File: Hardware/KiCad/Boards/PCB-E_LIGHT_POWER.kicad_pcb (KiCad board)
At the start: 2 copper layers, 110 x 94 mm, 0 parts

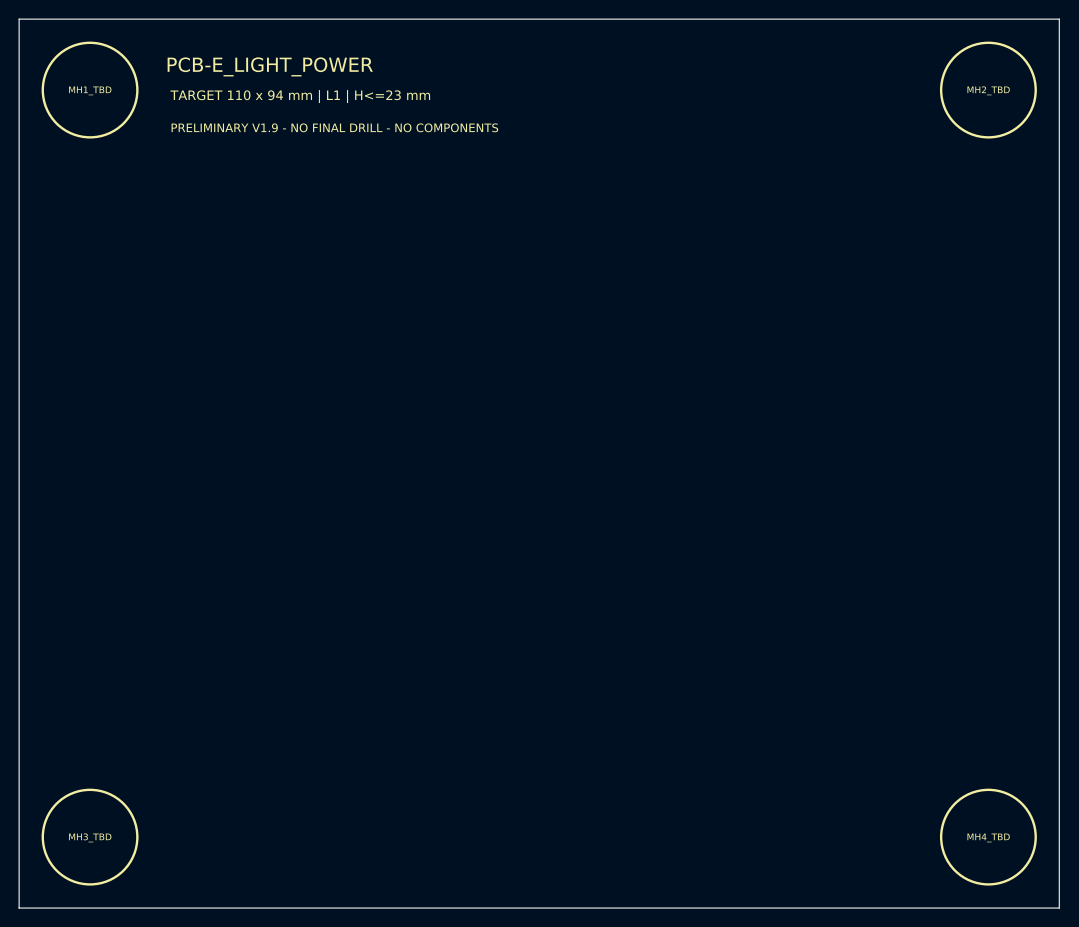
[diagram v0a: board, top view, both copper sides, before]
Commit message: hardware: add PCB-E functional, height and thermal placeholders
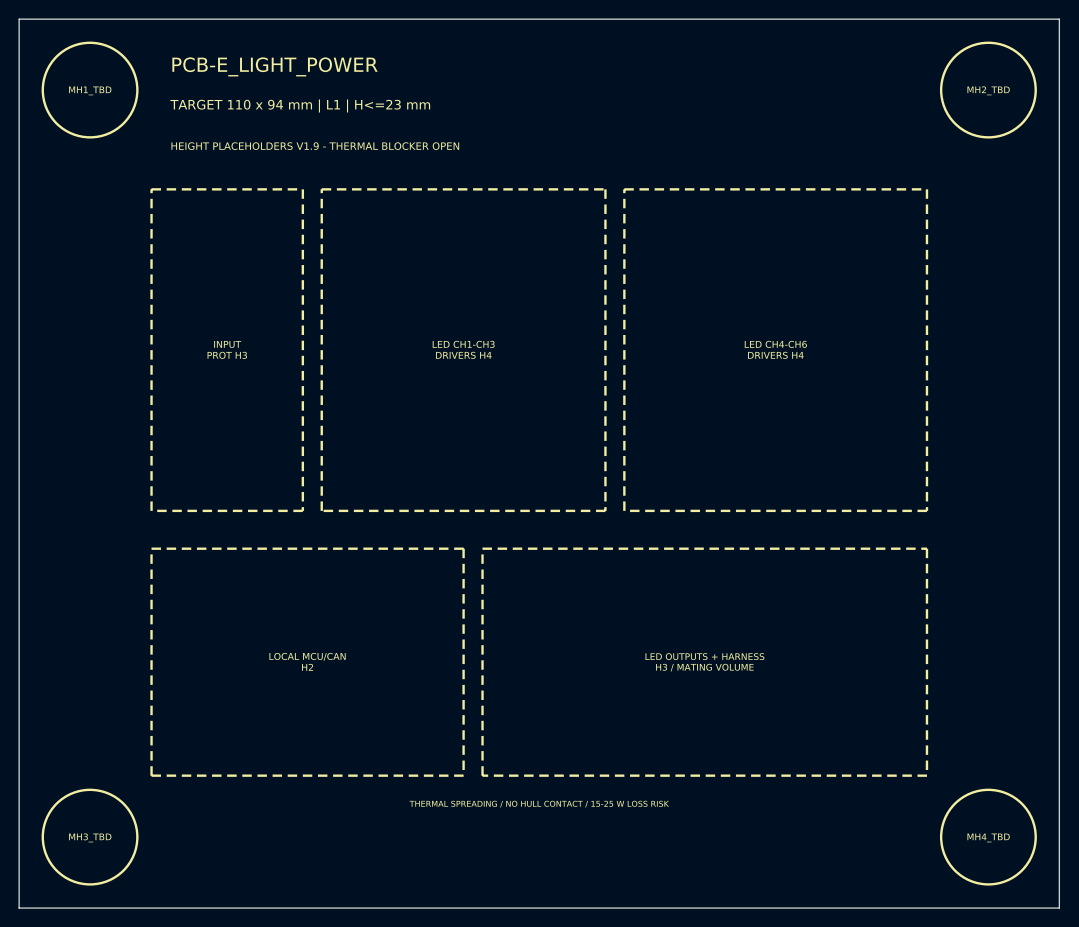
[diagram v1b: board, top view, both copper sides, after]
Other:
- board text added: "HEIGHT PLACEHOLDERS V1.9 - THERMAL BLOCKER OPEN"
- board text added: "INPUT PROT H3"
- board text added: "LED CH1-CH3 DRIVERS H4"
- board text added: "LED CH4-CH6 DRIVERS H4"
- board text added: "LED OUTPUTS + HARNESS H3 / MATING VOLUME"
- board text added: "LOCAL MCU/CAN H2"
- board text added: "THERMAL SPREADING / NO HULL CONTACT / 15-25 W LOSS RISK"
- board text removed: "PRELIMINARY V1.9 - NO FINAL DRILL - NO COMPONENTS"
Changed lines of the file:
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@@
 		(pad_to_mask_clearance 0)
 		(allow_soldermask_bridges_in_footprints no)
-		(tenting
-			(front yes)
-			(back yes)
-		)
-		(covering
-			(front no)
-			(back no)
-		)
-		(plugging
-			(front no)
-			(back no)
-		)
-		(capping no)
-		(filling no)
-		(pcbplotparams
-			(layerselection 0x00000000_00000000_55555555_5755f5ff)
-			(plot_on_all_layers_selection 0x00000000_00000000_00000000_00000000)
-			(disableapertmacros no)
-			(usegerberextensions no)
-			(usegerberattributes yes)
-			(usegerberadvancedattributes yes)
-			(creategerberjobfile yes)
-			(dashed_line_dash_ratio 12)
-			(dashed_line_gap_ratio 3)
-			(svgprecision 4)
-			(plotframeref no)
-			(mode 1)
-			(useauxorigin no)
-			(pdf_front_fp_property_popups yes)
-			(pdf_back_fp_property_popups yes)
-			(pdf_metadata yes)
-			(pdf_single_document no)
-			(dxfpolygonmode yes)
-			(dxfimperialunits yes)
-			(dxfusepcbnewfont yes)
-			(psnegative no)
-			(psa4output no)
-			(plot_black_and_white yes)
-			(sketchpadsonfab no)
-			(plotpadnumbers no)
-			(hidednponfab no)
-			(sketchdnponfab yes)
-			(crossoutdnponfab yes)
-			(subtractmaskfromsilk no)
-			(outputformat 1)
-			(mirror no)
-			(drillshape 1)
-			(scaleselection 1)
-			(outputdirectory "")
-		)
 	)
-	(gr_circle
-		(center 27.5 27.5)
-		(end 32.5 27.5)
-		(stroke
-			(width 0.25)
-			(type dash)
-		)
-		(fill no)
-		(layer "F.SilkS")
-	)
-	(gr_circle
-		(center 27.5 106.5)
-		(end 32.5 106.5)
-		(stroke
-			(width 0.25)
-			(type dash)
-		)
-		(fill no)
-		(layer "F.SilkS")
-	)
-	(gr_circle
-		(center 122.5 27.5)
-		(end 127.5 27.5)
-		(stroke
-			(width 0.25)
-			(type dash)
-		)
-		(fill no)
-		(layer "F.SilkS")
-	)
-	(gr_circle
-		(center 122.5 106.5)
-		(end 127.5 106.5)
-		(stroke
-			(width 0.25)
-			(type dash)
-		)
-		(fill no)
-		(layer "F.SilkS")
-	)
-	(gr_rect
-		(start 20 20)
-		(end 130 114)
-		(stroke
-			(width 0.05)
-			(type default)
-		)
-		(fill no)
-		(layer "Edge.Cuts")
-	)
-	(gr_text "MH1_TBD"
-		(at 27.5 27.5 0)
-		(layer "F.SilkS")
-		(effects
-			(font
-				(size 0.7 0.7)
-				(thickness 0.14)
-			)
-		)
-	)
-	(gr_text "MH3_TBD"
-		(at 27.5 106.5 0)
-		(layer "F.SilkS")
-		(effects
-			(font
-				(size 0.7 0.7)
-				(thickness 0.14)
-			)
-		)
-	)
-	(gr_text "MH2_TBD"
-		(at 122.5 27.5 0)
-		(layer "F.SilkS")
-		(effects
-			(font
-				(size 0.7 0.7)
-				(thickness 0.14)
-			)
-		)
-	)
-	(gr_text "MH4_TBD"
-		(at 122.5 106.5 0)
-		(layer "F.SilkS")
-		(effects
-			(font
-				(size 0.7 0.7)
-				(thickness 0.14)
-			)
-		)
-	)
-	(gr_text "PRELIMINARY V1.9 - NO FINAL DRILL - NO COMPONENTS"
-		(at 36 31 0)
-		(layer "F.SilkS")
-		(effects
-			(font
-				(size 0.9 0.9)
-				(thickness 0.18)
-			)
-			(justify left top)
-		)
-	)
-	(gr_text "TARGET 110 x 94 mm | L1 | H<=23 mm"
-		(at 36 27.5 0)
-		(layer "F.SilkS")
-		(effects
-			(font
-				(size 1 1)
-				(thickness 0.2)
-			)
-			(justify left top)
-		)
-	)
-	(gr_text "PCB-E_LIGHT_POWER"
-		(at 35.5 24 0)
-		(layer "F.SilkS")
-		(effects
-			(font
-				(size 1.5 1.5)
-				(thickness 0.3)
-			)
-			(justify left top)
-		)
-	)
+	(gr_rect (start 20 20) (end 130 114) (stroke (width 0.05) (type default)) (fill no) (layer "Edge.Cuts"))
+	(gr_text "PCB-E_LIGHT_POWER" (at 36 24 0) (layer "F.SilkS") (effects (font (size 1.5 1.5) (thickness 0.3)) (justify left top)))
+	(gr_text "TARGET 110 x 94 mm | L1 | H<=23 mm" (at 36 28.5 0) (layer "F.SilkS") (effects (font (size 1 1) (thickness 0.2)) (justify left top)))
+	(gr_text "HEIGHT PLACEHOLDERS V1.9 - THERMAL BLOCKER OPEN" (at 36 33 0) (layer "F.SilkS") (effects (font (size 0.78 0.78) (thickness 0.15)) (justify left top)))
+	(gr_circle (center 27.5 27.5) (end 32.5 27.5) (stroke (width 0.25) (type dash)) (fill no) (layer "F.SilkS"))
+	(gr_circle (center 27.5 106.5) (end 32.5 106.5) (stroke (width 0.25) (type dash)) (fill no) (layer "F.SilkS"))
+	(gr_circle (center 122.5 27.5) (end 127.5 27.5) (stroke (width 0.25) (type dash)) (fill no) (layer "F.SilkS"))
+	(gr_circle (center 122.5 106.5) (end 127.5 106.5) (stroke (width 0.25) (type dash)) (fill no) (layer "F.SilkS"))
+	(gr_text "MH1_TBD" (at 27.5 27.5 0) (layer "F.SilkS") (effects (font (size 0.7 0.7) (thickness 0.14))))
+	(gr_text "MH2_TBD" (at 122.5 27.5 0) (layer "F.SilkS") (effects (font (size 0.7 0.7) (thickness 0.14))))
+	(gr_text "MH3_TBD" (at 27.5 106.5 0) (layer "F.SilkS") (effects (font (size 0.7 0.7) (thickness 0.14))))
+	(gr_text "MH4_TBD" (at 122.5 106.5 0) (layer "F.SilkS") (effects (font (size 0.7 0.7) (thickness 0.14))))
+	(gr_rect (start 34 38) (end 50 72) (stroke (width 0.25) (type dash)) (fill no) (layer "F.SilkS"))
+	(gr_text "INPUT\nPROT H3" (at 42 55 0) (layer "F.SilkS") (effects (font (size 0.72 0.72) (thickness 0.13))))
+	(gr_rect (start 52 38) (end 82 72) (stroke (width 0.25) (type dash)) (fill no) (layer "F.SilkS"))
+	(gr_text "LED CH1-CH3\nDRIVERS H4" (at 67 55 0) (layer "F.SilkS") (effects (font (size 0.72 0.72) (thickness 0.13))))
+	(gr_rect (start 84 38) (end 116 72) (stroke (width 0.25) (type dash)) (fill no) (layer "F.SilkS"))
+	(gr_text "LED CH4-CH6\nDRIVERS H4" (at 100 55 0) (layer "F.SilkS") (effects (font (size 0.72 0.72) (thickness 0.13))))
+	(gr_rect (start 34 76) (end 67 100) (stroke (width 0.25) (type dash)) (fill no) (layer "F.SilkS"))
+	(gr_text "LOCAL MCU/CAN\nH2" (at 50.5 88 0) (layer "F.SilkS") (effects (font (size 0.72 0.72) (thickness 0.13))))
+	(gr_rect (start 69 76) (end 116 100) (stroke (width 0.25) (type dash)) (fill no) (layer "F.SilkS"))
+	(gr_text "LED OUTPUTS + HARNESS\nH3 / MATING VOLUME" (at 92.5 88 0) (layer "F.SilkS") (effects (font (size 0.7 0.7) (thickness 0.13))))
+	(gr_rect (start 32 36) (end 118 102) (stroke (width 0.3) (type dash)) (fill no) (layer "Margin"))
+	(gr_text "THERMAL SPREADING / NO HULL CONTACT / 15-25 W LOSS RISK" (at 75 103 0) (layer "F.SilkS") (effects (font (size 0.62 0.62) (thickness 0.12))))
 	(embedded_fonts no)
 )
